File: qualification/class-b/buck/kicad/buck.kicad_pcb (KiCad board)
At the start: 4 copper layers, 67.5 x 48 mm, 27 parts, among them J1 24V_IN, J2 3V3_OUT, U1 LMR33640ADDA

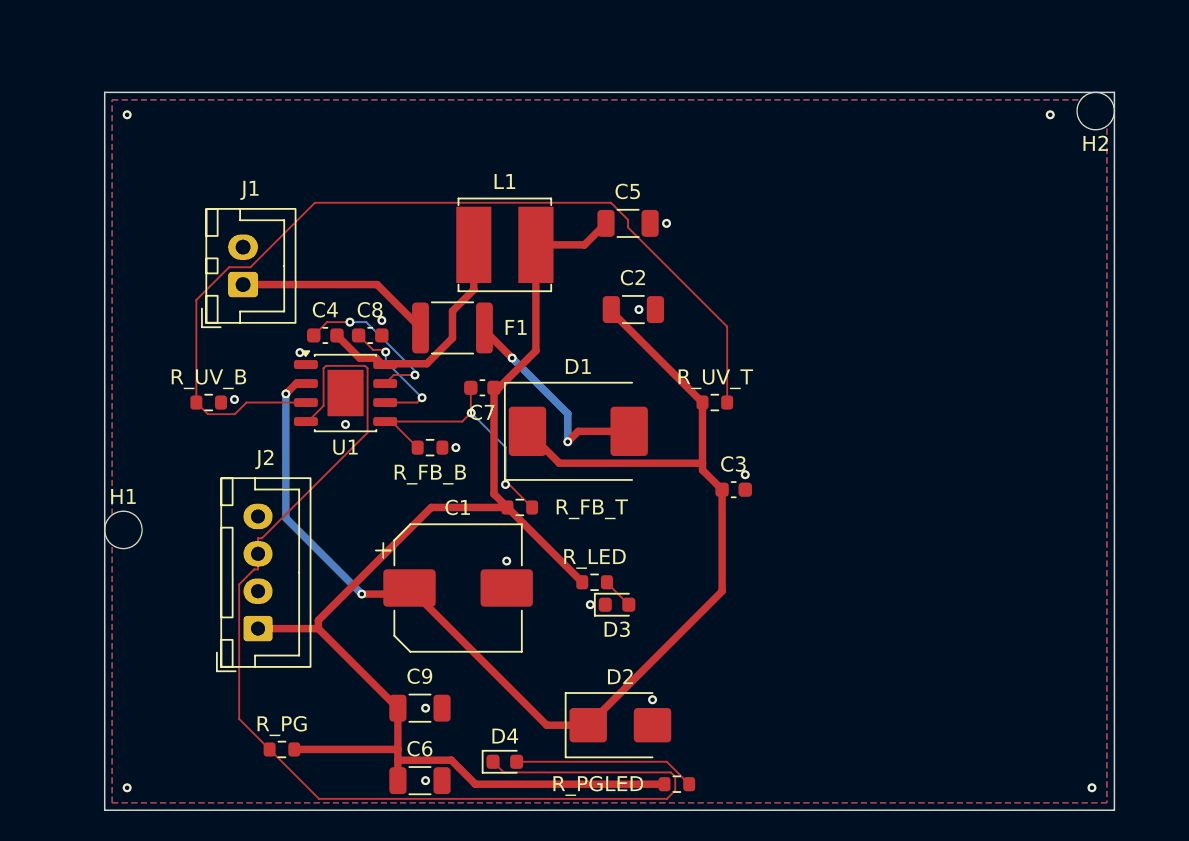
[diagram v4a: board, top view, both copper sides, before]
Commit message: SYN-67 - Put J1 and J2 on the board edges and let Synth place the rest
J1 and J2 get hard edge hints (left and right) and the sidecar is gone, so the mounting holes are no longer pinned at the old corners. The placer now fits a 60.85 x 31.09 mm board (1892 mm2) that routes with 0 open nets and 0 DRC errors. Adds the angled 3D, bottom 3D and top and bottom copper images and regenerates the KiCad files, reports, hashes and docs.

Signed-off-by: nyagamunene <stevenyaga2014@gmail.com>
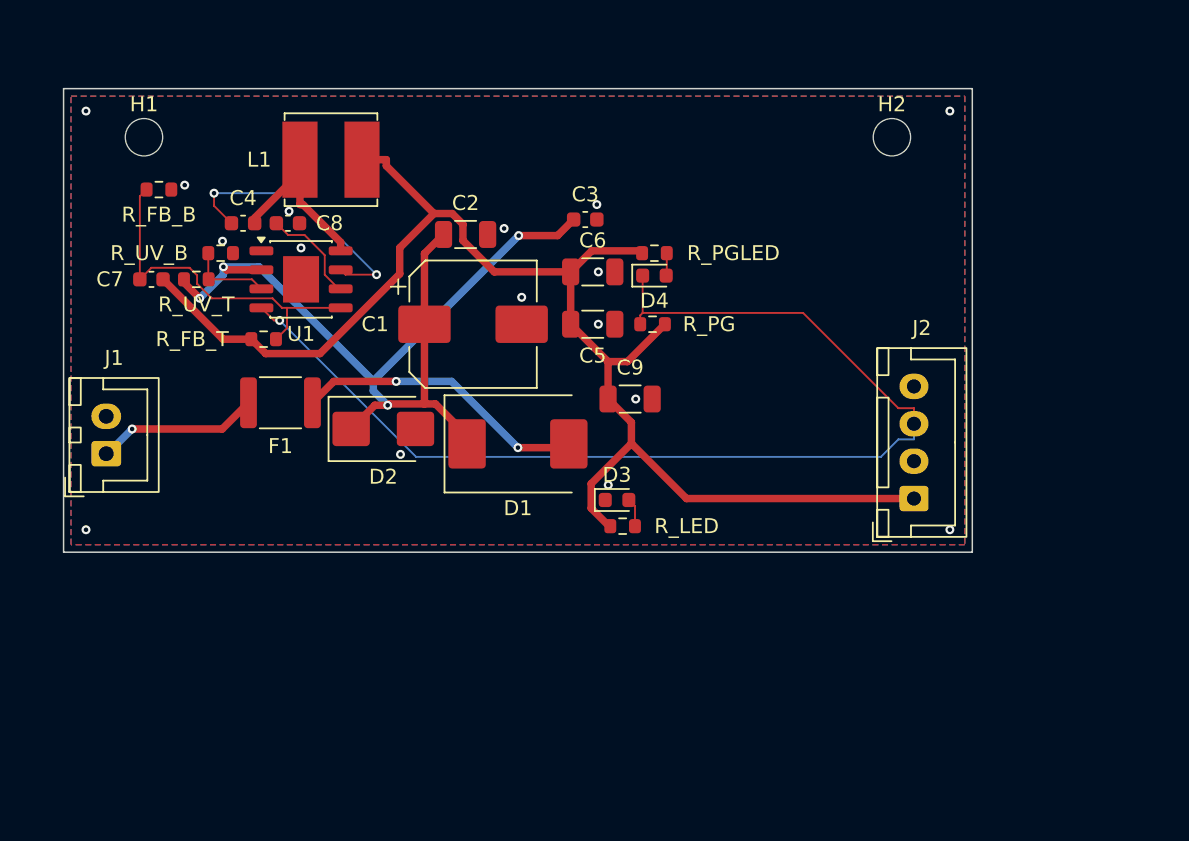
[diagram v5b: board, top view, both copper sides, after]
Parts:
- moved J2 44.7 mm to (56.9, 29.9)
- moved R_PG 37.7 mm to (39.4, 18.2)
- moved C6 35.9 mm to (35.4, 14.8)
- moved R_UV_T 35.6 mm to (8.88, 15.2)
- moved R_PGLED 35.5 mm to (39.5, 13.5)
- moved D4 34.0 mm to (39.5, 15.0)
- moved H1 26.3 mm to (5.38, 5.75)
- moved D2 25.4 mm to (21.4, 25.2)
- moved R_FB_B 25.0 mm to (6.38, 9.25)
- moved C9 25.0 mm to (37.9, 23.2)
- moved C7 23.3 mm to (5.88, 15.2)
- moved C3 20.6 mm to (34.9, 11.2)
- moved R_FB_T 20.5 mm to (13.4, 19.2)
- moved C1 17.7 mm to (27.4, 18.2)
- moved J1 14.5 mm to (2.85, 26.9)
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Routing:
- net EN: track 61.8 -> 5.55 mm
- net VIN: track 83.4 -> 61.9 mm, vias 2 -> 4
- net LED_PG: track 12.2 -> 1.52 mm
- net BOOT: track 11.0 -> 18.1 mm
- net VIN_FUSED: track 14.3 -> 19.7 mm
- net FB: track 18.5 -> 23.8 mm, vias 2 -> 0
- net PG: track 79.6 -> 74.4 mm, vias 0 -> 1
- net +3V3: track 89.8 -> 94.1 mm
- net SW: track 16.1 -> 12.0 mm
- net VIN_RAW: track 13.1 -> 10.9 mm, vias 0 -> 1
- net U1_VCC: track 8.93 -> 6.88 mm, vias 2 -> 0
- net GND: vias 17 -> 16
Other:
- board size 67.5 x 48 mm -> 60.8 x 31 mm

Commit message: SYN-67 - Restore the hand-placed buck layout and regenerate it on current main
Re-exported on main 2054046: routes with 0 open nets and 0 DRC errors, 81 segments, 16 vias, 230.50 mm. KiCad files, reports, 3D renders, hashes and docs regenerated. Copper and schematic images are carried over from f805d61.

Signed-off-by: nyagamunene <stevenyaga2014@gmail.com>
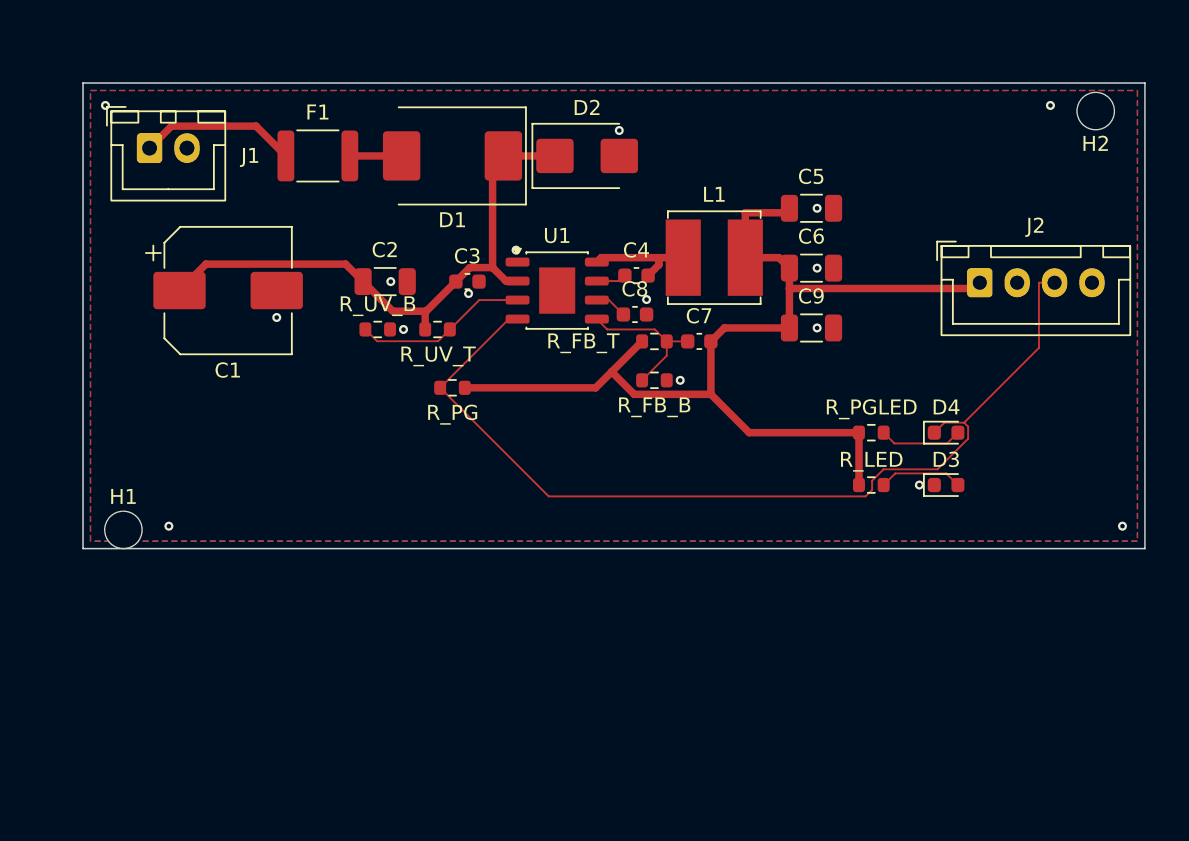
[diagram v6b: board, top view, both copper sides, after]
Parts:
- moved C7 36.9 mm to (42.5, 19.4)
- moved R_FB_B 35.5 mm to (39.5, 22.0)
- moved C4 26.5 mm to (38.3, 15.0)
- moved L1 26.4 mm to (43.5, 13.8)
- moved H1 26.3 mm to (4.00, 32.0)
- moved R_FB_T 26.1 mm to (39.5, 19.4)
- moved C8 24.0 mm to (38.2, 17.6)
- moved D2 22.8 mm to (35.0, 7.00)
- moved D4 22.1 mm to (59.0, 25.5)
- moved D3 22.0 mm to (59.0, 29.0)
- moved J1 20.6 mm to (5.75, 6.47), turned to 0 degrees
- moved D1 19.7 mm to (26.0, 7.00), turned to 180 degrees
- moved R_PGLED 18.8 mm to (54.0, 25.5)
- moved U1 17.1 mm to (33.0, 16.0)
- moved R_LED 16.9 mm to (54.0, 29.0)
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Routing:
- net +3V3: track 94.1 -> 70.2 mm
- net VIN: track 61.9 -> 38.6 mm, vias 4 -> 0
- net VIN_FUSED: track 19.7 -> 3.46 mm, vias 2 -> 0
- net BOOT: track 18.1 -> 2.03 mm, vias 2 -> 0
- net FB: track 23.8 -> 9.98 mm
- net PG: track 74.4 -> 63.2 mm, vias 1 -> 0
- net EN: track 5.55 -> 11.6 mm
- net U1_VCC: track 6.88 -> 2.17 mm
- net SW: track 12.0 -> 7.40 mm
- net LED_PG: track 1.52 -> 5.56 mm
- net LED_PWR: track 1.92 -> 5.61 mm
- net VIN_RAW: track 10.9 -> 10.5 mm, vias 1 -> 0
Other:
- board size 60.8 x 31 mm -> 71 x 31.1 mm

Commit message: SYN-67 - Place the buck board with Synth's own placer and regenerate the evidence on one head
Signed-off-by: nyagamunene <stevenyaga2014@gmail.com>
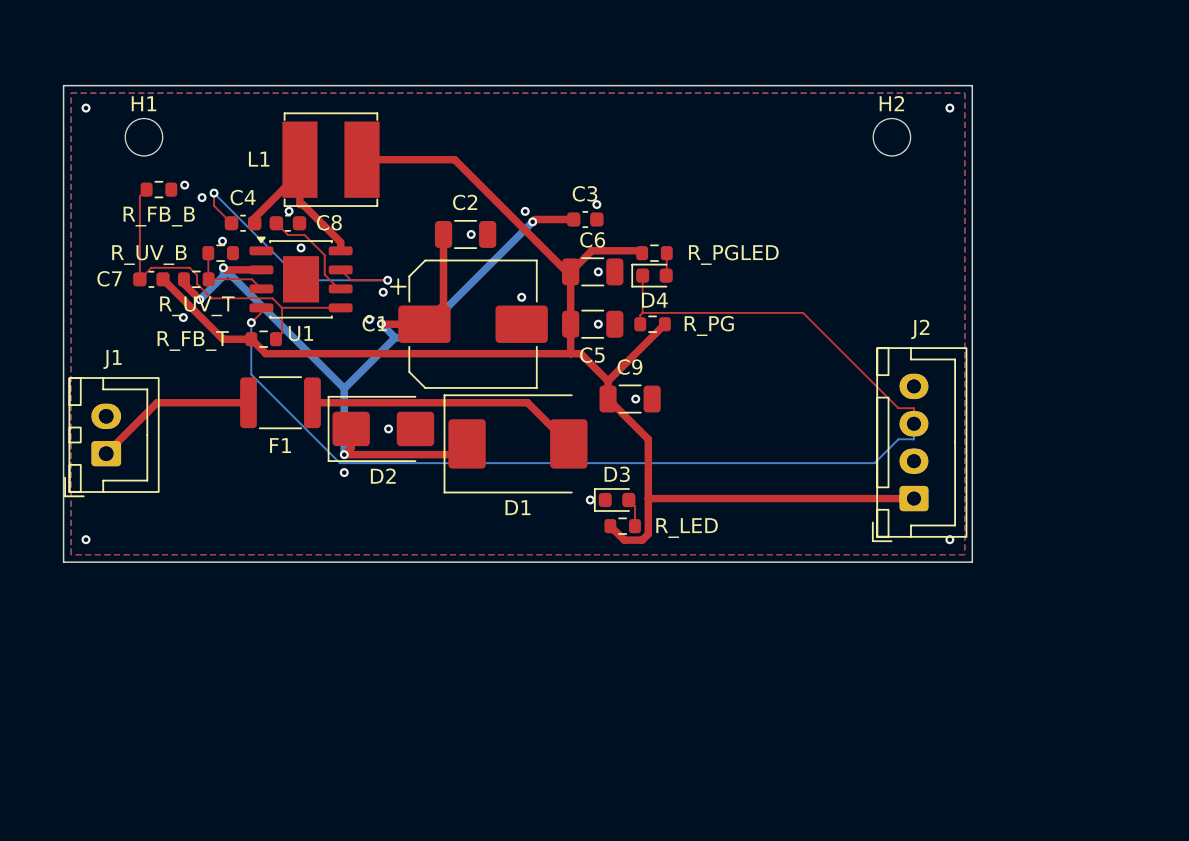
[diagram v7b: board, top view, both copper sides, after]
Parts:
- moved C7 36.9 mm to (5.88, 15.2)
- moved R_FB_B 35.5 mm to (6.38, 9.25)
- moved C4 26.5 mm to (12.0, 11.5)
- moved L1 26.4 mm to (17.9, 7.25)
- moved H1 26.3 mm to (5.38, 5.75)
- moved R_FB_T 26.1 mm to (13.4, 19.2)
- moved C8 24.0 mm to (15.0, 11.5)
- moved D2 22.8 mm to (21.4, 25.2)
- moved D4 22.1 mm to (39.5, 15.0)
- moved D3 22.0 mm to (37.0, 30.0)
- moved J1 20.6 mm to (2.85, 26.9), turned to 90 degrees
- moved D1 19.7 mm to (30.4, 26.2), turned to 0 degrees
- moved R_PGLED 18.8 mm to (39.5, 13.5)
- moved U1 17.1 mm to (15.9, 15.2)
- moved R_LED 16.9 mm to (37.4, 31.8)
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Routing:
- net +3V3: track 70.2 -> 98.1 mm
- net VIN: track 38.6 -> 64.2 mm, vias 0 -> 5
- net BOOT: track 2.03 -> 20.0 mm, vias 0 -> 2
- net PG: track 63.2 -> 78.3 mm, vias 0 -> 1
- net VIN_FUSED: track 3.46 -> 18.3 mm
- net FB: track 9.98 -> 23.6 mm
- net EN: track 11.6 -> 5.55 mm
- net U1_VCC: track 2.17 -> 6.88 mm
- net SW: track 7.40 -> 12.0 mm
- net LED_PG: track 5.56 -> 1.52 mm
- net LED_PWR: track 5.61 -> 1.92 mm
- net GND: vias 16 -> 22
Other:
- board size 71 x 31.1 mm -> 60.8 x 31.9 mm
- rule via_min_size: 0.6 -> 0.56

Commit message: SYN-67 - Regenerate the buck artifacts and rewrite the evidence for the LMR38010 board, add the matrix row
Signed-off-by: nyagamunene <stevenyaga2014@gmail.com>
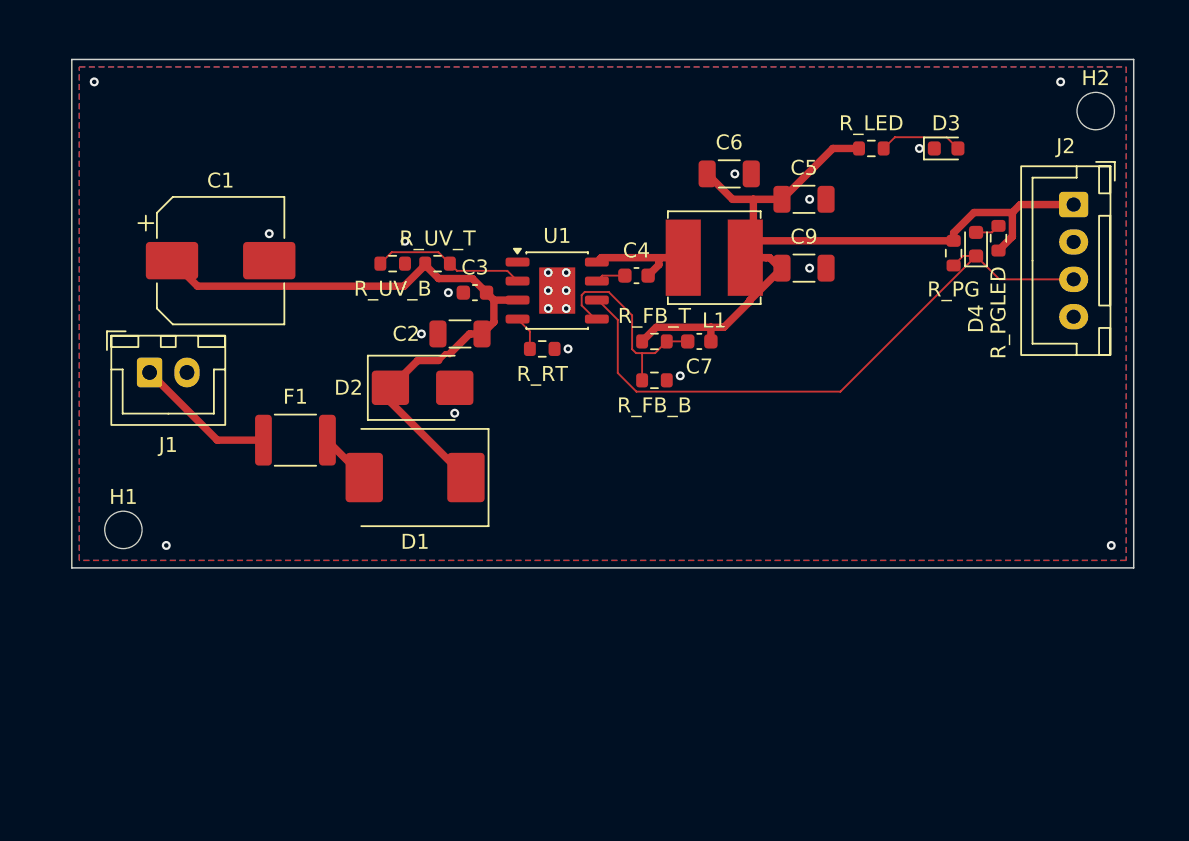
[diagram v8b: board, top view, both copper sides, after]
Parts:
- removed C8: 1uF, Capacitor_SMD:C_0603_1608Metric
- added R_RT: 33k, Resistor_SMD:R_0603_1608Metric, F.Cu at (32.0, 19.9)
- U1: value LMR33640ADDA -> LMR38010SDDAR
- moved C7 36.9 mm to (42.5, 19.4)
- moved R_FB_B 35.5 mm to (39.5, 22.0)
- moved D3 32.2 mm to (59.0, 6.50)
- moved R_LED 30.2 mm to (54.0, 6.50)
- moved C4 26.5 mm to (38.3, 15.0)
- moved L1 26.4 mm to (43.5, 13.8)
- moved H1 26.3 mm to (4.00, 32.0)
- moved R_FB_T 26.1 mm to (39.5, 19.4)
- moved R_PGLED 23.0 mm to (62.5, 12.5), turned to 90 degrees
- moved J2 22.4 mm to (67.5, 10.2), turned to 270 degrees
- moved D4 21.6 mm to (61.0, 12.9), turned to 90 degrees
- moved R_PG 20.7 mm to (59.5, 13.5), turned to 90 degrees
- moved C1 17.4 mm to (10.5, 14.0)
- moved U1 17.1 mm to (33.0, 16.0)
- moved C5 16.4 mm to (49.5, 9.90)
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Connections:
- U1 pad 2: VIN -> EN
- U1 pad 3: EN -> VIN
- U1 pad 4: PG -> RT
- U1 pad 6: U1_VCC -> PG
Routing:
- net +3V3: track 98.1 -> 56.9 mm
- net PG: track 78.3 -> 42.7 mm, vias 1 -> 0
- net VIN: track 64.2 -> 43.8 mm, vias 5 -> 0
- net BOOT: track 20.0 -> 2.03 mm, vias 2 -> 0
- net VIN_FUSED: track 18.3 -> 3.52 mm
- net FB: track 23.6 -> 14.4 mm
- net U1_VCC: track 6.88 -> 0.00 mm
- net EN: track 5.55 -> 10.3 mm
- net SW: track 12.0 -> 7.40 mm
- net LED_PWR: track 1.92 -> 5.58 mm
- net RT: track 0.00 -> 2.34 mm
- net VIN_RAW: track 10.9 -> 9.49 mm
- net GND: vias 22 -> 21
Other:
- board size 60.8 x 31.9 mm -> 71 x 34 mm
